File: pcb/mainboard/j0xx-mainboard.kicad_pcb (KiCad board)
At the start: 2 copper layers, 67.5 x 63.2 mm, 35 parts, among them J1 USB_C_Receptacle, J2 Conn_01x07, J3 Conn_01x05, J4 Conn_01x04, J5 Conn_01x08, J6 Conn_01x10, Q1 BSS138, SW1 reset, U1 ATmega32U4-AU, Y1 Resonator

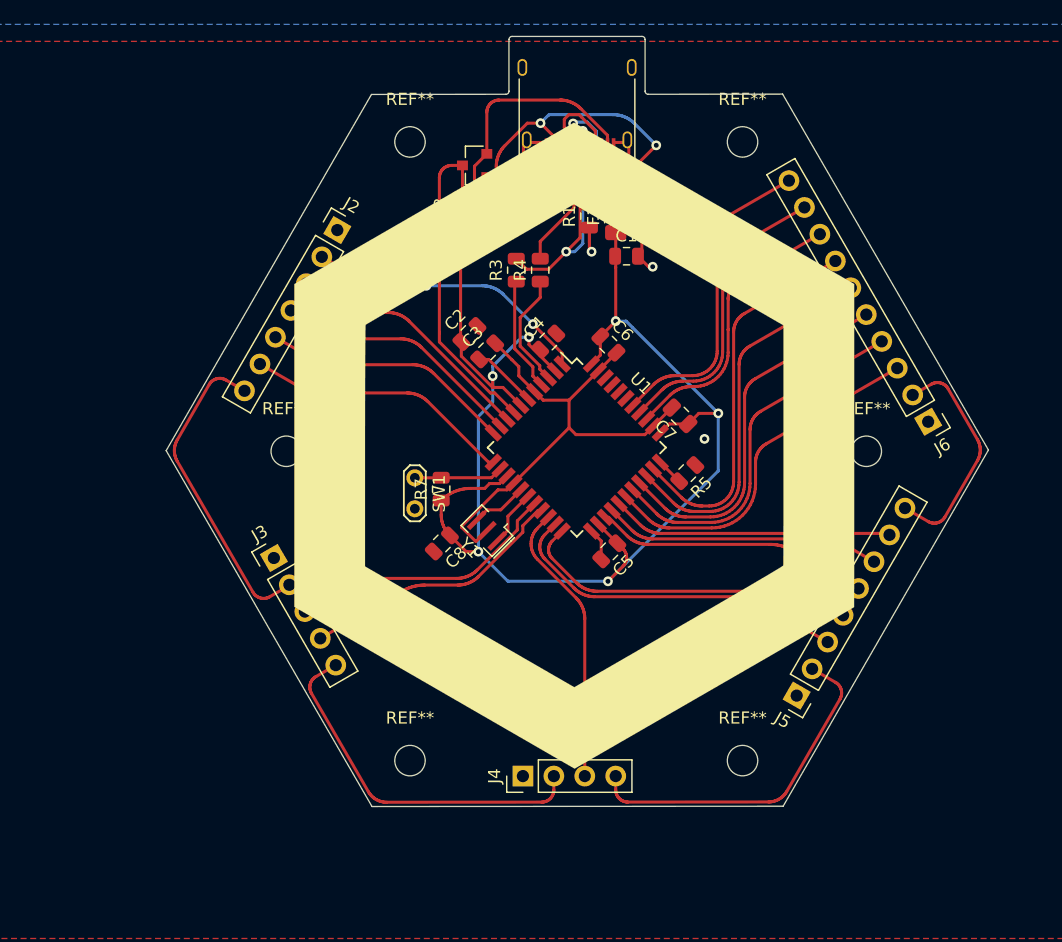
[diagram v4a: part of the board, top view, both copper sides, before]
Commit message: Add most PCB modules
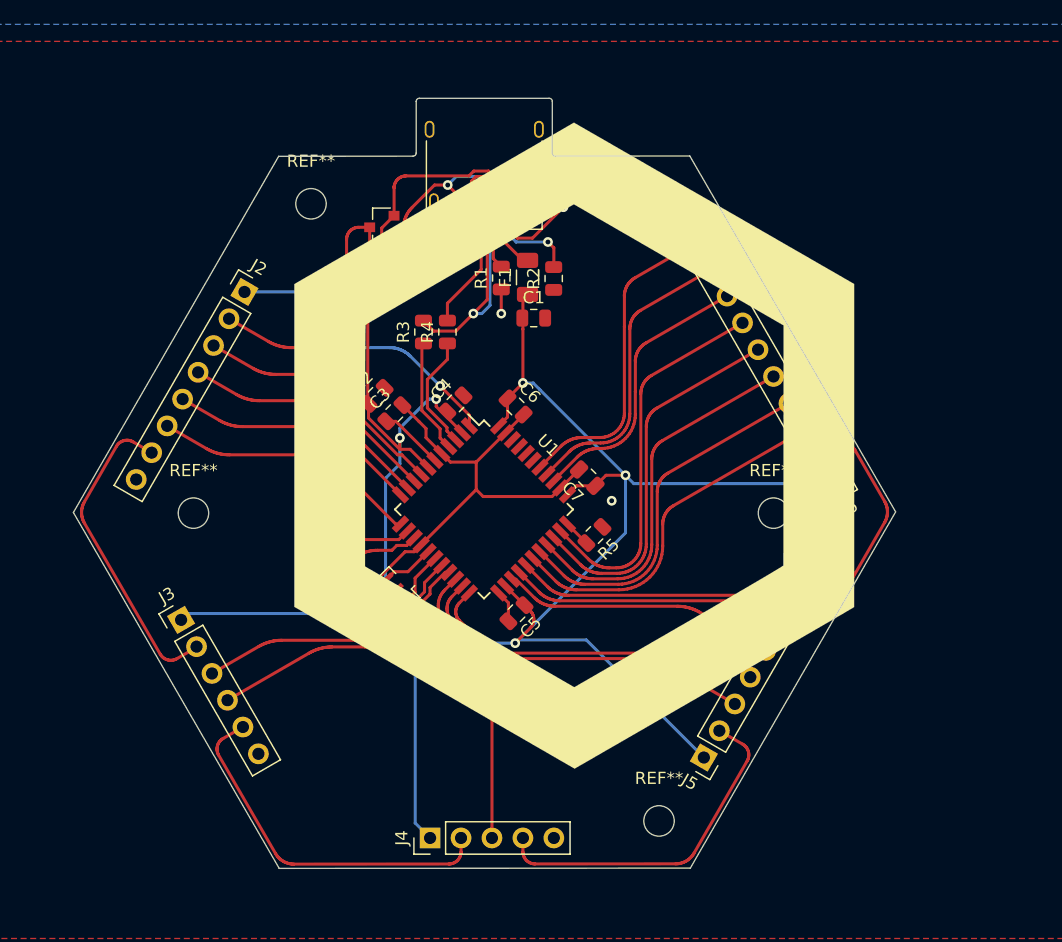
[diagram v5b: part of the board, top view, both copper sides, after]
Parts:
- removed the REF** at (198.1, 118.7)
- removed the REF** at (225.4, 67.9)
- J2: value Conn_01x07 -> Conn_01x08; footprint Connector_PinHeader_2.54mm:PinHeader_1x07_P2.54mm_Vertical -> Connector_PinHeader_2.54mm:PinHeader_1x08_P2.54mm_Vertical
- J3: value Conn_01x05 -> Conn_01x06; footprint Connector_PinHeader_2.54mm:PinHeader_1x05_P2.54mm_Vertical -> Connector_PinHeader_2.54mm:PinHeader_1x06_P2.54mm_Vertical
- J4: value Conn_01x04 -> Conn_01x05; footprint Connector_PinHeader_2.54mm:PinHeader_1x04_P2.54mm_Vertical -> Connector_PinHeader_2.54mm:PinHeader_1x05_P2.54mm_Vertical
- J5: value Conn_01x08 -> Conn_01x09; footprint Connector_PinHeader_2.54mm:PinHeader_1x08_P2.54mm_Vertical -> Connector_PinHeader_2.54mm:PinHeader_1x09_P2.54mm_Vertical
- J6: value Conn_01x10 -> Conn_01x11; footprint Connector_PinHeader_2.54mm:PinHeader_1x10_P2.54mm_Vertical -> Connector_PinHeader_2.54mm:PinHeader_1x11_P2.54mm_Vertical
- moved REF** 9.58 mm to (190.0, 73.0)
- moved C1 9.16 mm to (208.3, 82.4)
- moved C8 9.16 mm to (193.1, 106.0)
- moved R5 9.16 mm to (213.3, 100.2)
- moved C2 9.16 mm to (195.4, 88.8)
- moved C3 9.16 mm to (196.8, 90.2)
- moved C4 9.16 mm to (201.9, 89.4)
- moved C5 9.16 mm to (206.9, 106.6)
- moved C7 9.16 mm to (212.7, 95.5)
- moved J1 9.16 mm to (204.2, 69.7)
- moved J2 9.16 mm to (184.5, 80.3)
- moved J4 9.16 mm to (199.8, 125.1)
- moved J5 9.16 mm to (222.2, 118.5)
- moved J6 9.16 mm to (233.0, 96.0)
- moved R3 9.16 mm to (199.2, 83.6)
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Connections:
- J2 pad 1: GND -> +5V
- J3 pad 1: GND -> +5V
- J4 pad 1: GND -> +5V
- J5 pad 1: GND -> +5V
- J6 pad 1: GND -> +5V
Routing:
- net +5V: track 118.0 -> 199.0 mm
- net GND: track 60.6 -> 55.7 mm, vias 3 -> 2
- net GCCD3.3v: track 30.2 -> 29.1 mm

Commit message: First full iteration of physical design
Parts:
- J1: footprint Connector_USB:USB_C_Receptacle_Amphenol_12401610E4-2A -> USB_C:USB_C_LCSC_C456013
- Y1: footprint Crystal:Resonator_SMD_muRata_CSTxExxV-3Pin_3.0x1.1mm -> Crystal:Resonator_SMD_Murata_CSTxExxV-3Pin_3.0x1.1mm
- moved G*** 9.28 mm to (204.2, 98.1)
- moved G*** 9.26 mm to (204.2, 98.1)
- moved J1 4.58 mm to (207.8, 72.5)
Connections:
- J1 pad A10: Net-(J1-PadA10) -> unconnected-(J1-PadA10)
- J1 pad A3: Net-(J1-PadA3) -> unconnected-(J1-PadA3)
- J1 pad A8: Net-(J1-PadA8) -> unconnected-(J1-PadA8)
- J1 pad B10: Net-(J1-PadB10) -> unconnected-(J1-PadB10)
- J1 pad B3: Net-(J1-PadB3) -> unconnected-(J1-PadB3)
- J1 pad B8: Net-(J1-PadB8) -> unconnected-(J1-PadB8)
- U1 pad 39: Net-(U1-Pad39) -> unconnected-(U1-Pad39)
- U1 pad 40: Net-(U1-Pad40) -> unconnected-(U1-Pad40)
- U1 pad 41: Net-(U1-Pad41) -> unconnected-(U1-Pad41)
- U1 pad 42: Net-(U1-Pad42) -> unconnected-(U1-Pad42)
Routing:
- net D-: track 11.2 -> 22.1 mm, vias 0 -> 1
- net GND: track 55.7 -> 51.7 mm
- net D+: track 24.8 -> 28.7 mm, vias 2 -> 1
- net Net-(F1-Pad2): track 13.5 -> 17.4 mm, vias 0 -> 2
- net Net-(J1-PadB5): track 13.3 -> 15.2 mm, vias 2 -> 1
- net Net-(J1-PadA5): track 3.68 -> 5.35 mm
- net +3V3: track 27.6 -> 29.1 mm, vias 2 -> 1
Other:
- net class Default removed
